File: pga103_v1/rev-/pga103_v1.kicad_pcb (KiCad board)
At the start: 2 copper layers, 34.3 x 40.6 mm, 28 parts, among them J1 RF_IN, J2 RF_OUT, J3 RFShield_TwoPieces, U1 SPX3819M5-L-5-0, U2 PGA-103

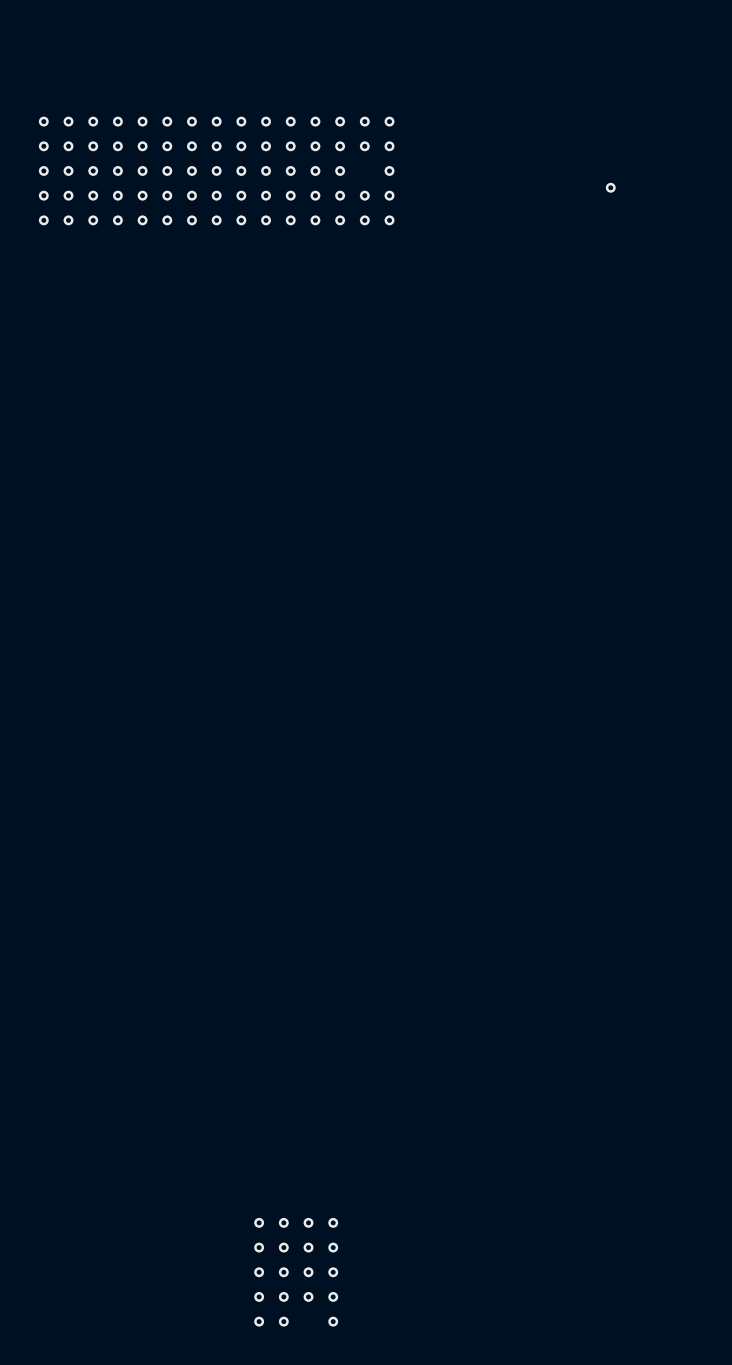
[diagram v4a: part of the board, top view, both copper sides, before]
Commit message: aded gitignore, about to rearrange for MAJOR.MINOR.PATCH versioning
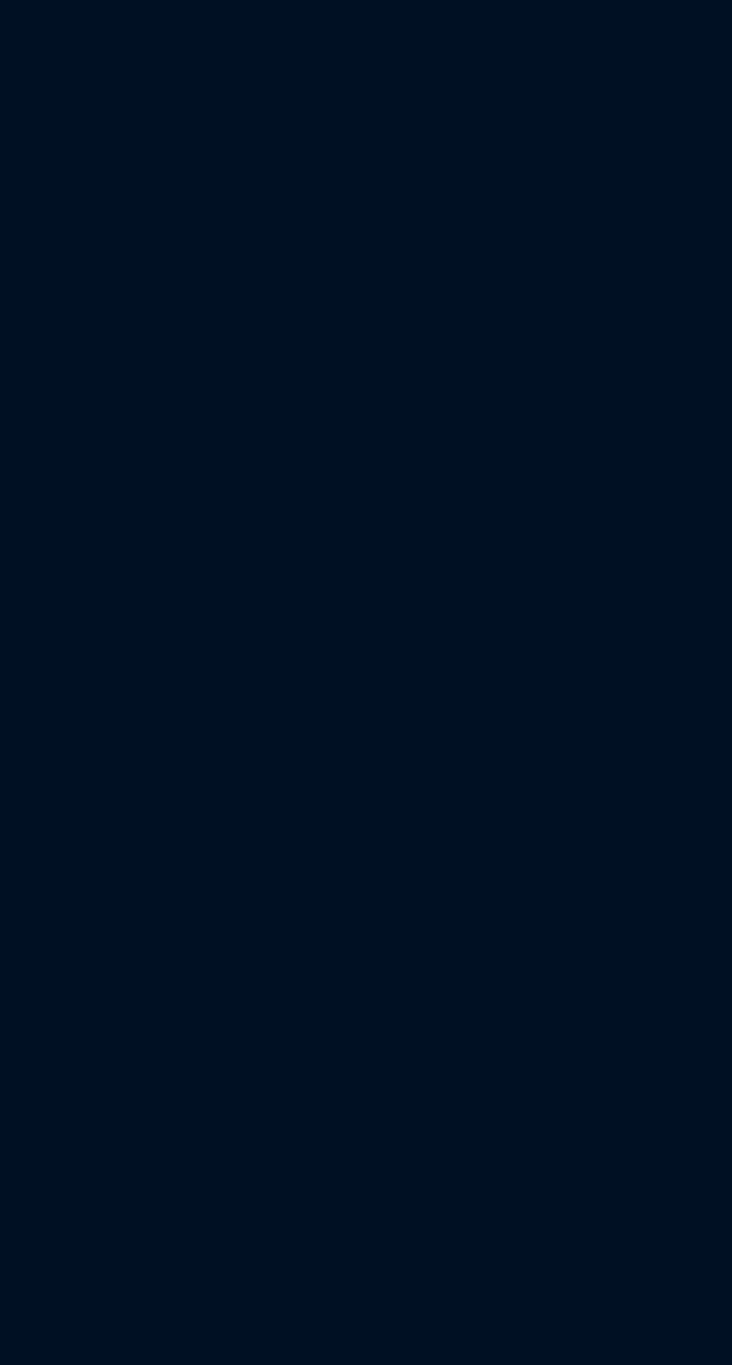
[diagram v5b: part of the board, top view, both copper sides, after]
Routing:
- net GND: vias 697 -> 603
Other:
- board text removed: "#2"
- board text removed: "0.75{dblquote}"
- board text removed: "1.0{dblquote}"
- board text removed: "1.25{dblquote}"
- board text removed: "1.5{dblquote}"
